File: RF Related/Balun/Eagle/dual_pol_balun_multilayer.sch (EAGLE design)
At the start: 8 parts, among them T1 ADT1-1WT+, T2 ADT1-1WT+, X1 SMA-142-0701-801/806, X2 SMA-142-0701-801/806, X3 SMA-142-0701-801/806, X4 SMA-142-0701-801/806, X5 SMA-142-0701-801/806, X6 SMA-142-0701-801/806

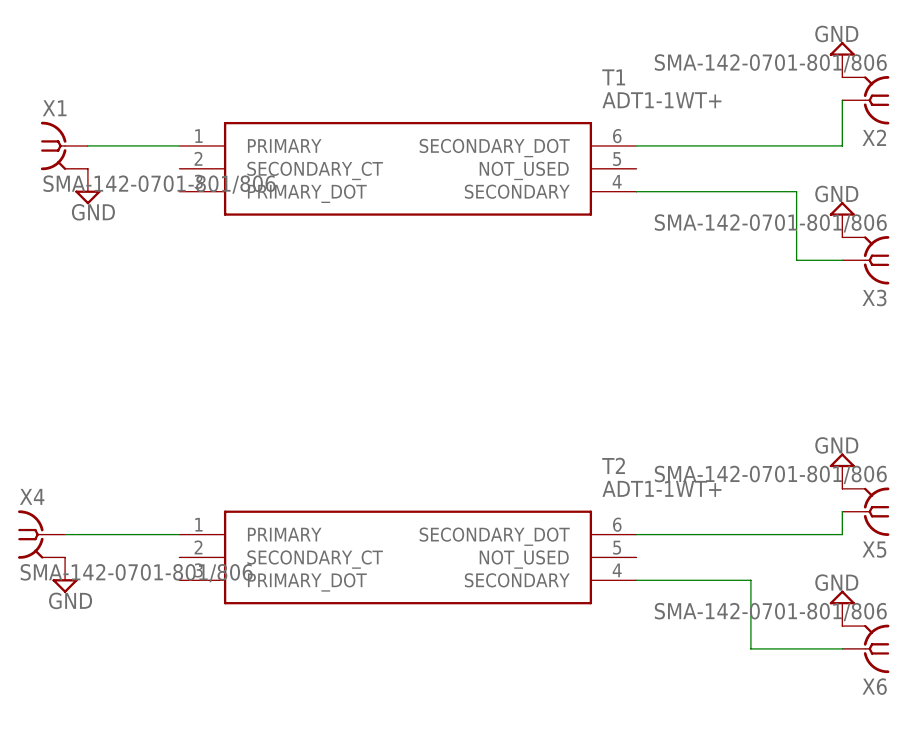
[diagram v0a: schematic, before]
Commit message: also updated entire drone 3D model to contain primary balun candidate.
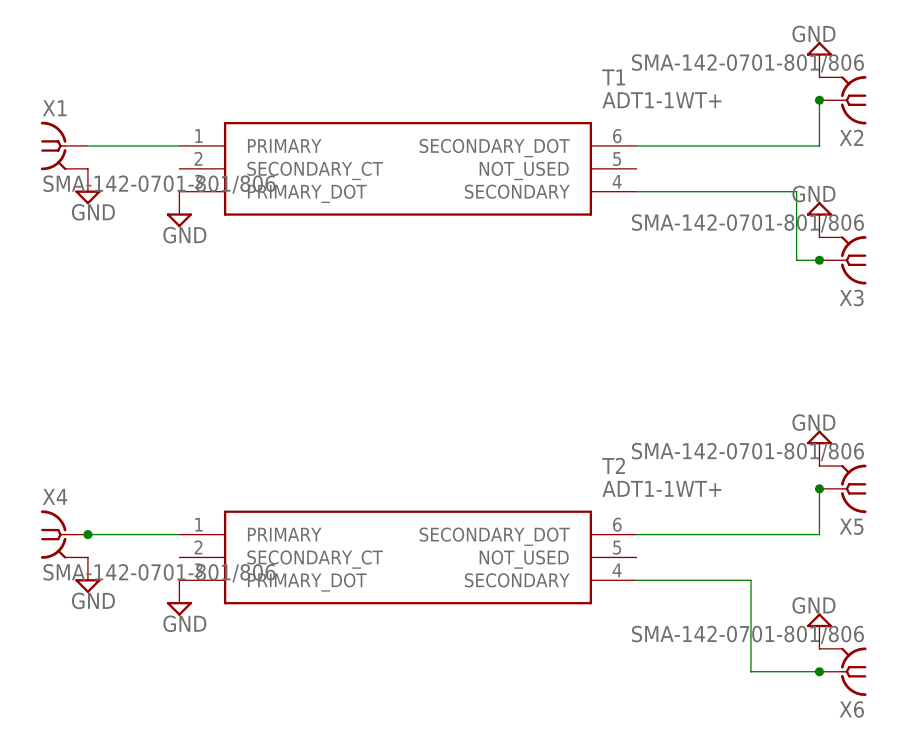
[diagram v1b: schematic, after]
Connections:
- net GND: now also T1.PRIMARY_DOT, T2.PRIMARY_DOT
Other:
- moved on the sheet: X2, X3, X4, X5, X6
